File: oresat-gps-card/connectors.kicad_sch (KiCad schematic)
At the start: 20 parts, among them J1 J-SAMTEC-TFM-120-01-L-D-RA, J3 J-TE-Debug-2-1734592-0

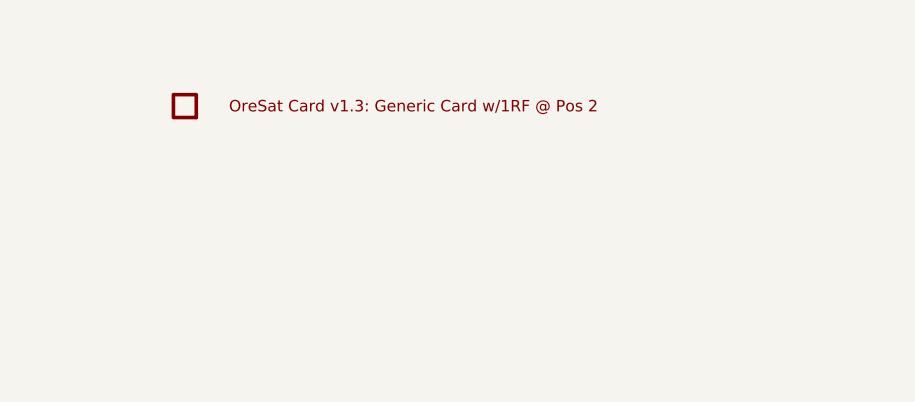
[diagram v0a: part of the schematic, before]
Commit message: GPS card design review changes and issue fixes
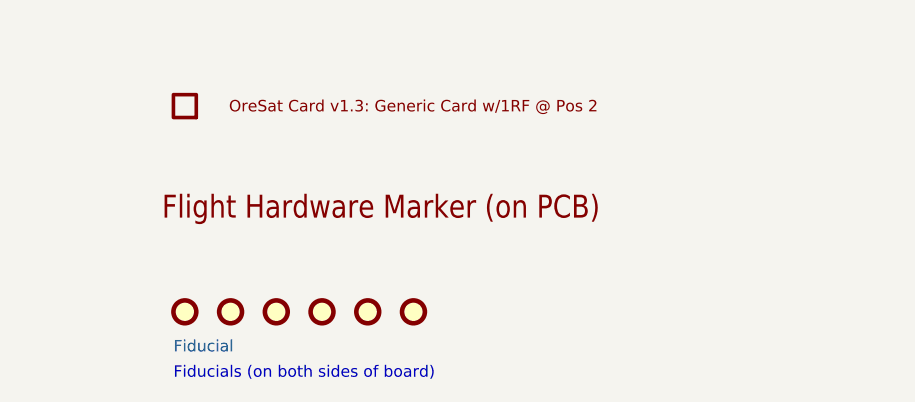
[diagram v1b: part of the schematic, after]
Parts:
- added FID1, FID2, FID3, FID4, FID5, FID6: Fiducial, oresat-misc:FIDUCIAL-1.0X2.0, symbol Mechanical:Fiducial
- added FLIGHT1: FLIGHTMARKER, oresat-graphics:FLIGHTMARKER, symbol oresat-graphics:FLIGHTMARKER
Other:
- note added: "Fiducials (on both sides of board)"
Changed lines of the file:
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@@
     (effects (font (size 2.54 2.159)) (justify right bottom))
+  )
+  (text "Fiducials (on both sides of board)" (at 153.67 256.54 0)
+    (effects (font (size 1.27 1.27)) (justify left bottom))
   )
   (text "Oresat Debug Connector" (at 254 76.2 180)
@@
     )
     (pin "1")
+  )
+  (symbol (lib_id "oresat-graphics:FLIGHTMARKER") (at 152.4 238.76 0) (unit 1)
+    (in_bom yes) (on_board yes) (fields_autoplaced)
+    (property "Reference" "FLIGHT1" (id 0) (at 152.4 238.76 0)
+      (effects (font (size 1.27 1.27)) hide)
+    )
+    (property "Value" "FLIGHTMARKER" (id 1) (at 152.4 238.76 0)
+      (effects (font (size 1.27 1.27)) hide)
+    )
+    (property "Footprint" "oresat-graphics:FLIGHTMARKER" (id 2) (at 152.4 238.76 0)
+      (effects (font (size 1.27 1.27)) hide)
+    )
+    (property "Datasheet" "" (id 3) (at 152.4 238.76 0)
+      (effects (font (size 1.27 1.27)) hide)
+    )
+  )
+  (symbol (lib_id "Mechanical:Fiducial") (at 165.1 248.92 0) (unit 1)
+    (in_bom yes) (on_board yes)
+    (property "Reference" "FID3" (id 0) (at 163.83 252.73 0)
+      (effects (font (size 1.27 1.27)) (justify left) hide)
+    )
+    (property "Value" "Fiducial" (id 1) (at 163.83 255.27 0)
+      (effects (font (size 1.27 1.27)) (justify left) hide)
+    )
+    (property "Footprint" "oresat-misc:FIDUCIAL-1.0X2.0" (id 2) (at 165.1 248.92 0)
+      (effects (font (size 1.27 1.27)) hide)
+    )
+    (property "Datasheet" "~" (id 3) (at 165.1 248.92 0)
+      (effects (font (size 1.27 1.27)) hide)
+    )
   )
   (symbol (lib_id "OreSat-Connectors:J-TE-Debug-2-1734592-0") (at 281.94 114.3 90) (unit 1)
@@
     (pin "PAD2")
   )
+  (symbol (lib_id "Mechanical:Fiducial") (at 170.18 248.92 0) (unit 1)
+    (in_bom yes) (on_board yes)
+    (property "Reference" "FID4" (id 0) (at 168.91 252.73 0)
+      (effects (font (size 1.27 1.27)) (justify left) hide)
+    )
+    (property "Value" "Fiducial" (id 1) (at 168.91 255.27 0)
+      (effects (font (size 1.27 1.27)) (justify left) hide)
+    )
+    (property "Footprint" "oresat-misc:FIDUCIAL-1.0X2.0" (id 2) (at 170.18 248.92 0)
+      (effects (font (size 1.27 1.27)) hide)
+    )
+    (property "Datasheet" "~" (id 3) (at 170.18 248.92 0)
+      (effects (font (size 1.27 1.27)) hide)
+    )
+  )
   (symbol (lib_id "OreSat-TestPoint:Test-Point") (at 96.52 96.52 270) (unit 1)
     (in_bom yes) (on_board yes)
@@
     )
     (pin "1")
+  )
+  (symbol (lib_id "Mechanical:Fiducial") (at 160.02 248.92 0) (unit 1)
+    (in_bom yes) (on_board yes)
+    (property "Reference" "FID2" (id 0) (at 158.75 252.73 0)
+      (effects (font (size 1.27 1.27)) (justify left) hide)
+    )
+    (property "Value" "Fiducial" (id 1) (at 158.75 255.27 0)
+      (effects (font (size 1.27 1.27)) (justify left) hide)
+    )
+    (property "Footprint" "oresat-misc:FIDUCIAL-1.0X2.0" (id 2) (at 160.02 248.92 0)
+      (effects (font (size 1.27 1.27)) hide)
+    )
+    (property "Datasheet" "~" (id 3) (at 160.02 248.92 0)
+      (effects (font (size 1.27 1.27)) hide)
+    )
   )
   (symbol (lib_id "OreSat-TestPoint:Test-Point") (at 96.52 104.14 270) (unit 1)
@@
     (pin "RF")
   )
+  (symbol (lib_id "Mechanical:Fiducial") (at 175.26 248.92 0) (unit 1)
+    (in_bom yes) (on_board yes)
+    (property "Reference" "FID5" (id 0) (at 173.99 252.73 0)
+      (effects (font (size 1.27 1.27)) (justify left) hide)
+    )
+    (property "Value" "Fiducial" (id 1) (at 173.99 255.27 0)
+      (effects (font (size 1.27 1.27)) (justify left) hide)
+    )
+    (property "Footprint" "oresat-misc:FIDUCIAL-1.0X2.0" (id 2) (at 175.26 248.92 0)
+      (effects (font (size 1.27 1.27)) hide)
+    )
+    (property "Datasheet" "~" (id 3) (at 175.26 248.92 0)
+      (effects (font (size 1.27 1.27)) hide)
+    )
+  )
   (symbol (lib_id "OreSat-TestPoint:Test-Point") (at 96.52 83.82 270) (unit 1)
     (in_bom yes) (on_board yes)
@@
     )
     (pin "1")
+  )
+  (symbol (lib_id "Mechanical:Fiducial") (at 180.34 248.92 0) (unit 1)
+    (in_bom yes) (on_board yes)
+    (property "Reference" "FID6" (id 0) (at 179.07 252.73 0)
+      (effects (font (size 1.27 1.27)) (justify left) hide)
+    )
+    (property "Value" "Fiducial" (id 1) (at 179.07 255.27 0)
+      (effects (font (size 1.27 1.27)) (justify left) hide)
+    )
+    (property "Footprint" "oresat-misc:FIDUCIAL-1.0X2.0" (id 2) (at 180.34 248.92 0)
+      (effects (font (size 1.27 1.27)) hide)
+    )
+    (property "Datasheet" "~" (id 3) (at 180.34 248.92 0)
+      (effects (font (size 1.27 1.27)) hide)
+    )
   )
   (symbol (lib_id "OreSat-TestPoint:Test-Point") (at 91.44 165.1 270) (unit 1)
@@
     (pin "1")
   )
+  (symbol (lib_id "Mechanical:Fiducial") (at 154.94 248.92 0) (unit 1)
+    (in_bom yes) (on_board yes)
+    (property "Reference" "FID1" (id 0) (at 153.67 252.73 0)
+      (effects (font (size 1.27 1.27)) (justify left) hide)
+    )
+    (property "Value" "Fiducial" (id 1) (at 153.67 252.73 0)
+      (effects (font (size 1.27 1.27)) (justify left))
+    )
+    (property "Footprint" "oresat-misc:FIDUCIAL-1.0X2.0" (id 2) (at 154.94 248.92 0)
+      (effects (font (size 1.27 1.27)) hide)
+    )
+    (property "Datasheet" "~" (id 3) (at 154.94 248.92 0)
+      (effects (font (size 1.27 1.27)) hide)
+    )
+  )
 )
